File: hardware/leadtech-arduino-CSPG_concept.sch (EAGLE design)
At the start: 51 parts, among them IC1 CD4050B, IC2 LM358D, J1 CON_HEADER_1X08-PTH, J2 CON_HEADER_1X08-PTH, J3 CON_HEADER_1X08-PTH, J4 CON_HEADER_1X06-PTH, J5 CON_HEADER_1X05-PTH, J6 CON_HEADER_1X02-PTH, J7 CON_HEADER_1X05-PTH, J8 CON_HEADER_1X08-PTH, J9 CON_HEADER_1X02-PTH, P1 CON_HEADER_2X09, P2 CON_HEADER_2X09, Q1 16Mhz, SW1 SW_TACT_2P-3X6, U1 DS1302, U2 MFRC522, U3 PL2303HX

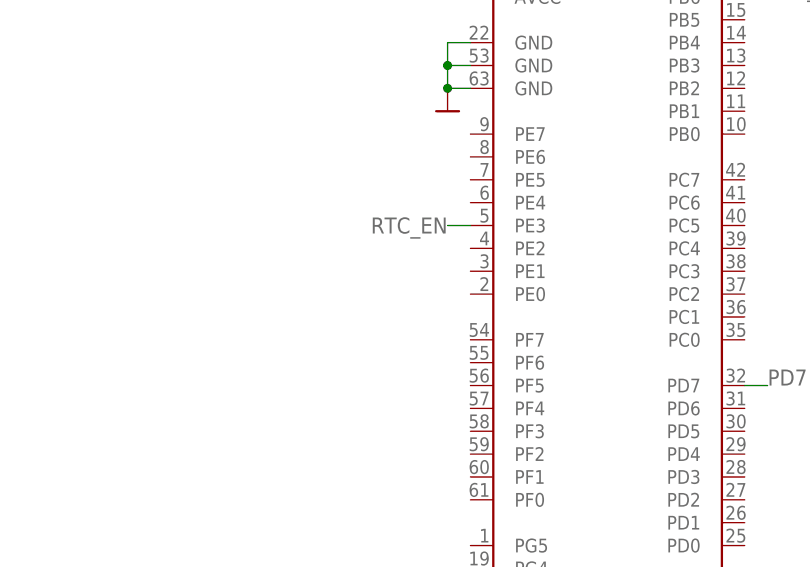
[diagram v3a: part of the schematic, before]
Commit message: continue wiring schematic
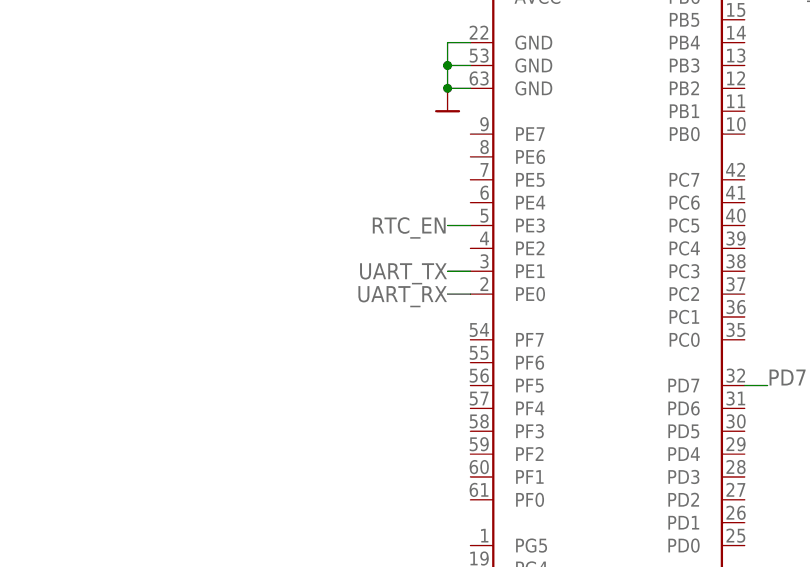
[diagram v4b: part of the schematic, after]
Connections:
- net UART_RX: now also U$1.PE0
- net UART_TX: now also U$1.PE1
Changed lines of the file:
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@@
 <label x="116.84" y="55.88" size="1.778" layer="95"/>
+</segment>
+<segment>
+<pinref part="U$1" gate="U" pin="PE0"/>
+<wire x1="383.54" y1="83.82" x2="381" y2="83.82" width="0.1524" layer="91"/>
+<label x="381" y="83.82" size="1.778" layer="95" align="center-right"/>
 </segment>
 </net>
@@
 <label x="116.84" y="48.26" size="1.778" layer="95"/>
 </segment>
+<segment>
+<pinref part="U$1" gate="U" pin="PE1"/>
+<wire x1="383.54" y1="86.36" x2="381" y2="86.36" width="0.1524" layer="91"/>
+<label x="381" y="86.36" size="1.778" layer="95" align="center-right"/>
+</segment>
 </net>

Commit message: add project schedule excel, add RFID module on schematic
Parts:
- removed U2: MFRC522, trosh_devices.eagle.v9:MFRC522
- added MOD1: RFIO-RC522, trosh_devices.eagle.v9:RFIO-RC522
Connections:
- net GND: now also MOD1.GND
- net N$1: now also MOD1.+3V3; no longer J8.8
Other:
- note added: "RFID MODULE"
- note added: "TO DO: wire RFID Module"
- note removed: "TO DO: connect RX and TX"
- moved on the sheet: C1, C10, G1, IC1P, R5, U1, XTAL1, ZD1

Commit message: continue wiring schematic, RFIF wiring done, level shifter done, add BOM with links on excel sheet
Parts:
- removed C1: 0.1uF, dp_devices.v6:CAPACITOR_NPOL-PTH_0.1"
- removed IC1: CD4050B, 40xx:4050N
- removed IC2: LM358D, linear:LM358D
- removed J7: CON_HEADER_1X05-PTH, dp_devices.v6:CON_HEADER_1X05-PTH
- removed J8: CON_HEADER_1X08-PTH, dp_devices.v6:CON_HEADER_1X08-PTH
- removed LED1: (no value), dp_devices.v6:LED-5MM
- removed R2: 4.7K, dp_devices.v6:RESISTOR-0603
- removed SW1: SW_TACT_2P-3X6, dp_devices.v6:SW_TACT_2P-3X6
- removed ZD1: 3.3V, dp_devices.v6:ZENERSOD-123
- added C14: 100uF, dp_devices.v6:CAPACITOR_POL-CASE_B
- added C15: 0.1uF, rcl:C-EUC0603
- added IC3: 4050D, 40xx:4050D
- added SG1: F/TMB, buzzer:F/TMB
- R1: value 330R -> 10K; device dp_devices.v6:RESISTOR-0603 -> rcl:R-EU_R0603
- R5: value 4.7K -> 10K; device dp_devices.v6:RESISTOR-0603 -> rcl:R-EU_R0603
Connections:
- removed net ARDUINO-10: IC1A.I, J1.3
- removed net ARDUINO-12: J1.5, J8.4
- removed net ARDUINO-2: J2.3, R2.2, SW1.1
- removed net ARDUINO-3: J2.4, R1.1
- removed net ARDUINO-5: J2.6, J7.5
- removed net ARDUINO-6: J2.7, J7.4
- removed net ARDUINO-7: J2.8, J7.3
- removed net ARDUINO-9: IC1D.I, J1.2
- removed net N$2: IC1A.O, J8.1
- removed net N$3: IC1B.I, J1.6
- removed net N$4: IC1B.O, J8.2
- removed net N$5: IC1C.I, J1.4
- removed net N$6: IC1C.O, J8.3
- removed net N$7: IC1D.O, J8.7
- removed net N$9: LED1.A, R1.2
- new net +3V3: C14.+, C15.2, IC3P.VDD, MOD1.+3V3
- new net OUT1: U$1.PE5
- new net PIEZO: R1.1, U$1.PG5
- new net RFID_CLOCK: IC3B.I, U$1.PB1
- new net RFID_CLOCK_3V: IC3B.O, MOD1.SCK
- new net RFID_DATA: IC3A.I, U$1.PB0
- new net RFID_DATA_3V: IC3A.O, MOD1.SDA
- new net RFID_MISO: MOD1.MISO, U$1.PB3
- new net RFID_MOSI: IC3C.I, U$1.PB2
- new net RFID_MOSI_3V: IC3C.O, MOD1.MOSI
- new net RFID_RESET: IC3D.I, U$1.PB5
- new net RFID_RESET_3V: IC3D.O, MOD1.RST
- new net SW1: R5.1, U$1.PE4
- net +5V: now also R5.2; no longer J7.1, LED2.A, R2.1, R5.1
- net GND: now also C14.-, C15.1, IC3P.VSS, SG1.-; no longer C1.2, IC1P.VSS, J7.2, J8.6, LED1.C, SW1.3, ZD1.A
- net N$1: now also R1.2, SG1.+; no longer C1.1, IC1P.VDD, MOD1.+3V3, R5.2, ZD1.C
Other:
- note added: "5V - 3.3V LEVEL SHIFTER"
- note added: "ARDUINO / ATMEGA1281"
- note added: "TO DO: change to HC-49S (PTH)"
- note added: "TO DO: place DC-DC power supply"
- note added: "TO DO: which USB connector?"
- note added: "VREGS"
- note removed: "3.3V"
- note removed: "CLK"
- note removed: "DAT"
- note removed: "IRQ"
- note removed: "MISO"
- note removed: "MOSI"
- note removed: "OUTPUT"
- note removed: "POWER SUPPLY"
- note removed: "RF-ID"
- note removed: "RST"
- note removed: "RTC"
- note removed: "SCK"
- note removed: "SDA"
- note removed: "SWITCH"
- note removed: "UC"
- moved on the sheet: C10, C8, C9, D1, G1, J9, LED2, MOD1, R9, U1, VREG1, XTAL1

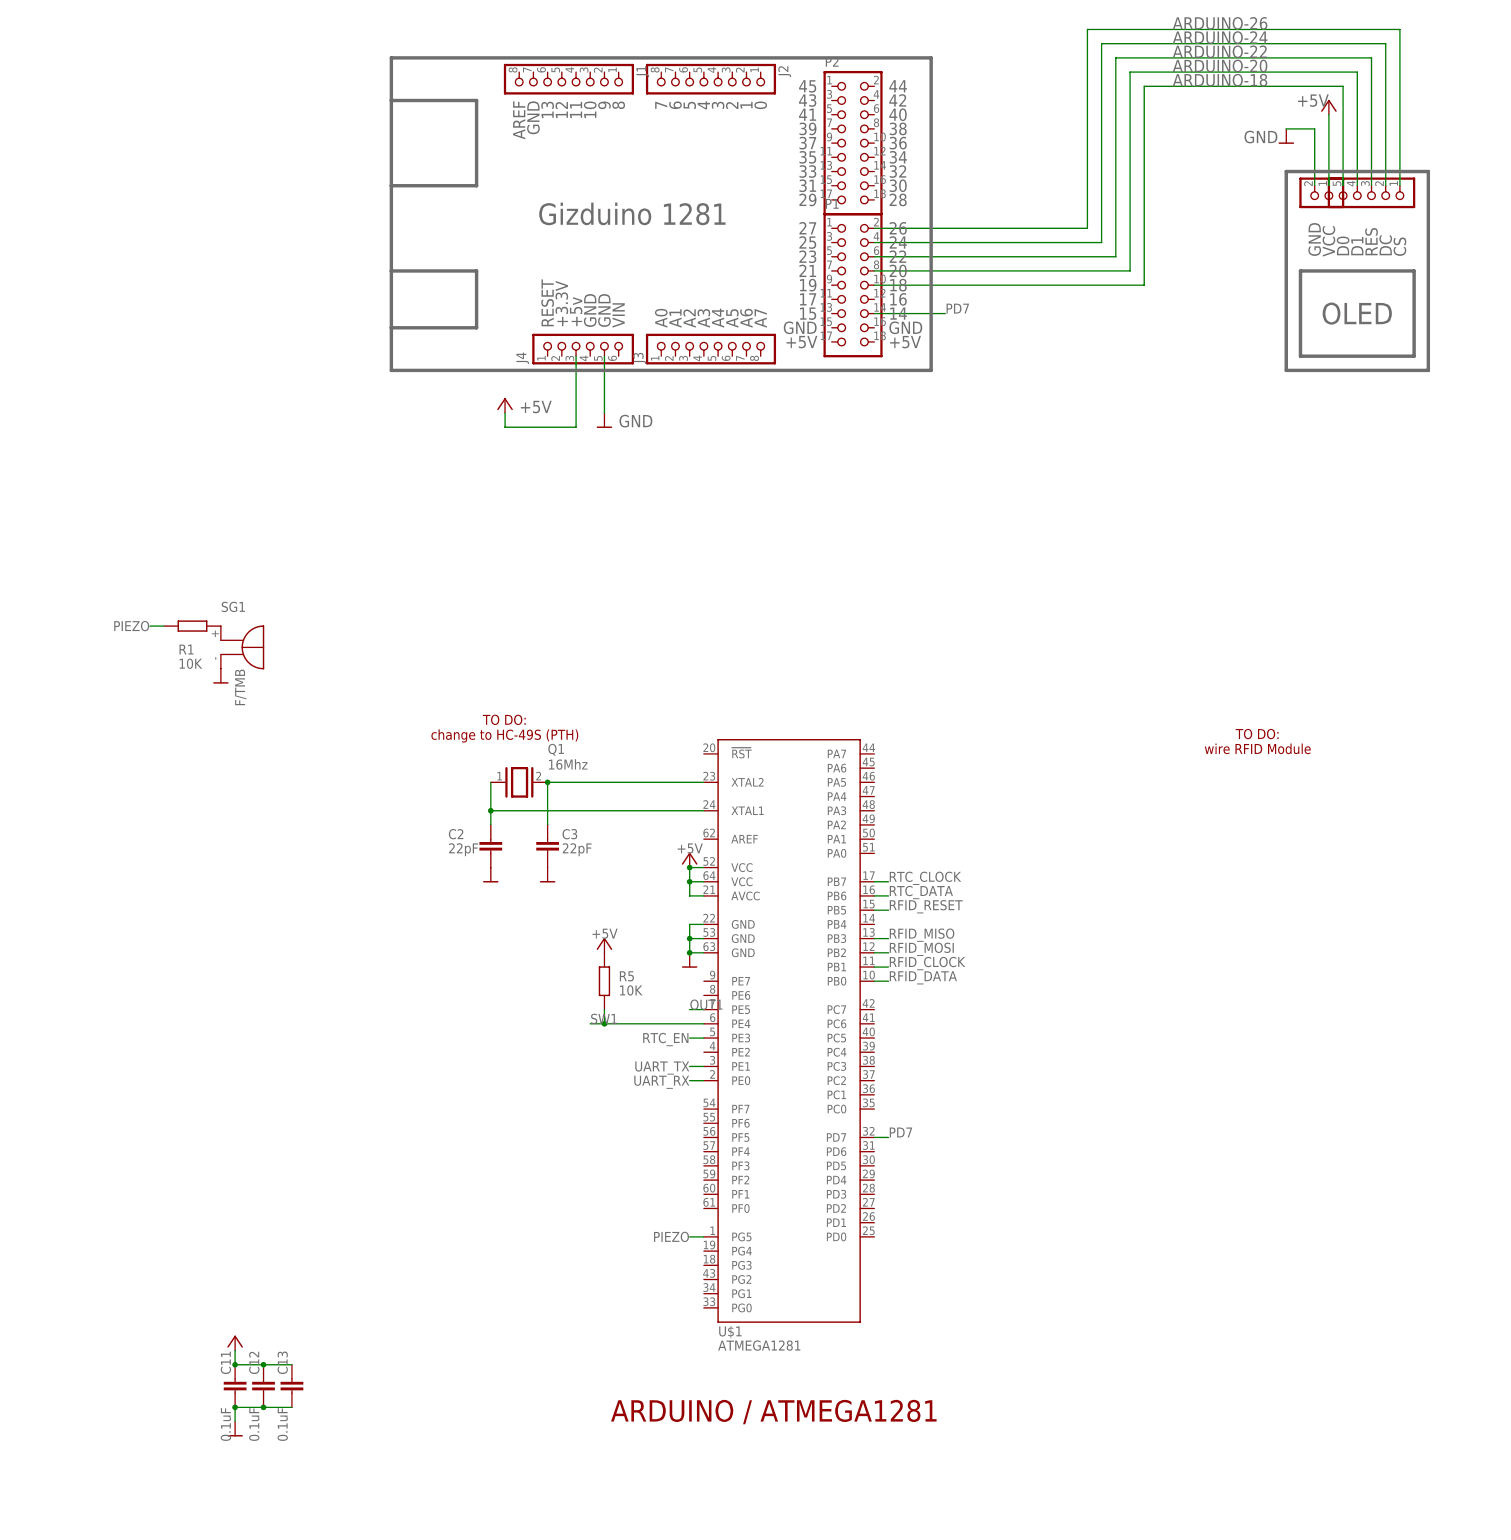
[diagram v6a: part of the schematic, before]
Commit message: continue on schematic work, add i2c OLED
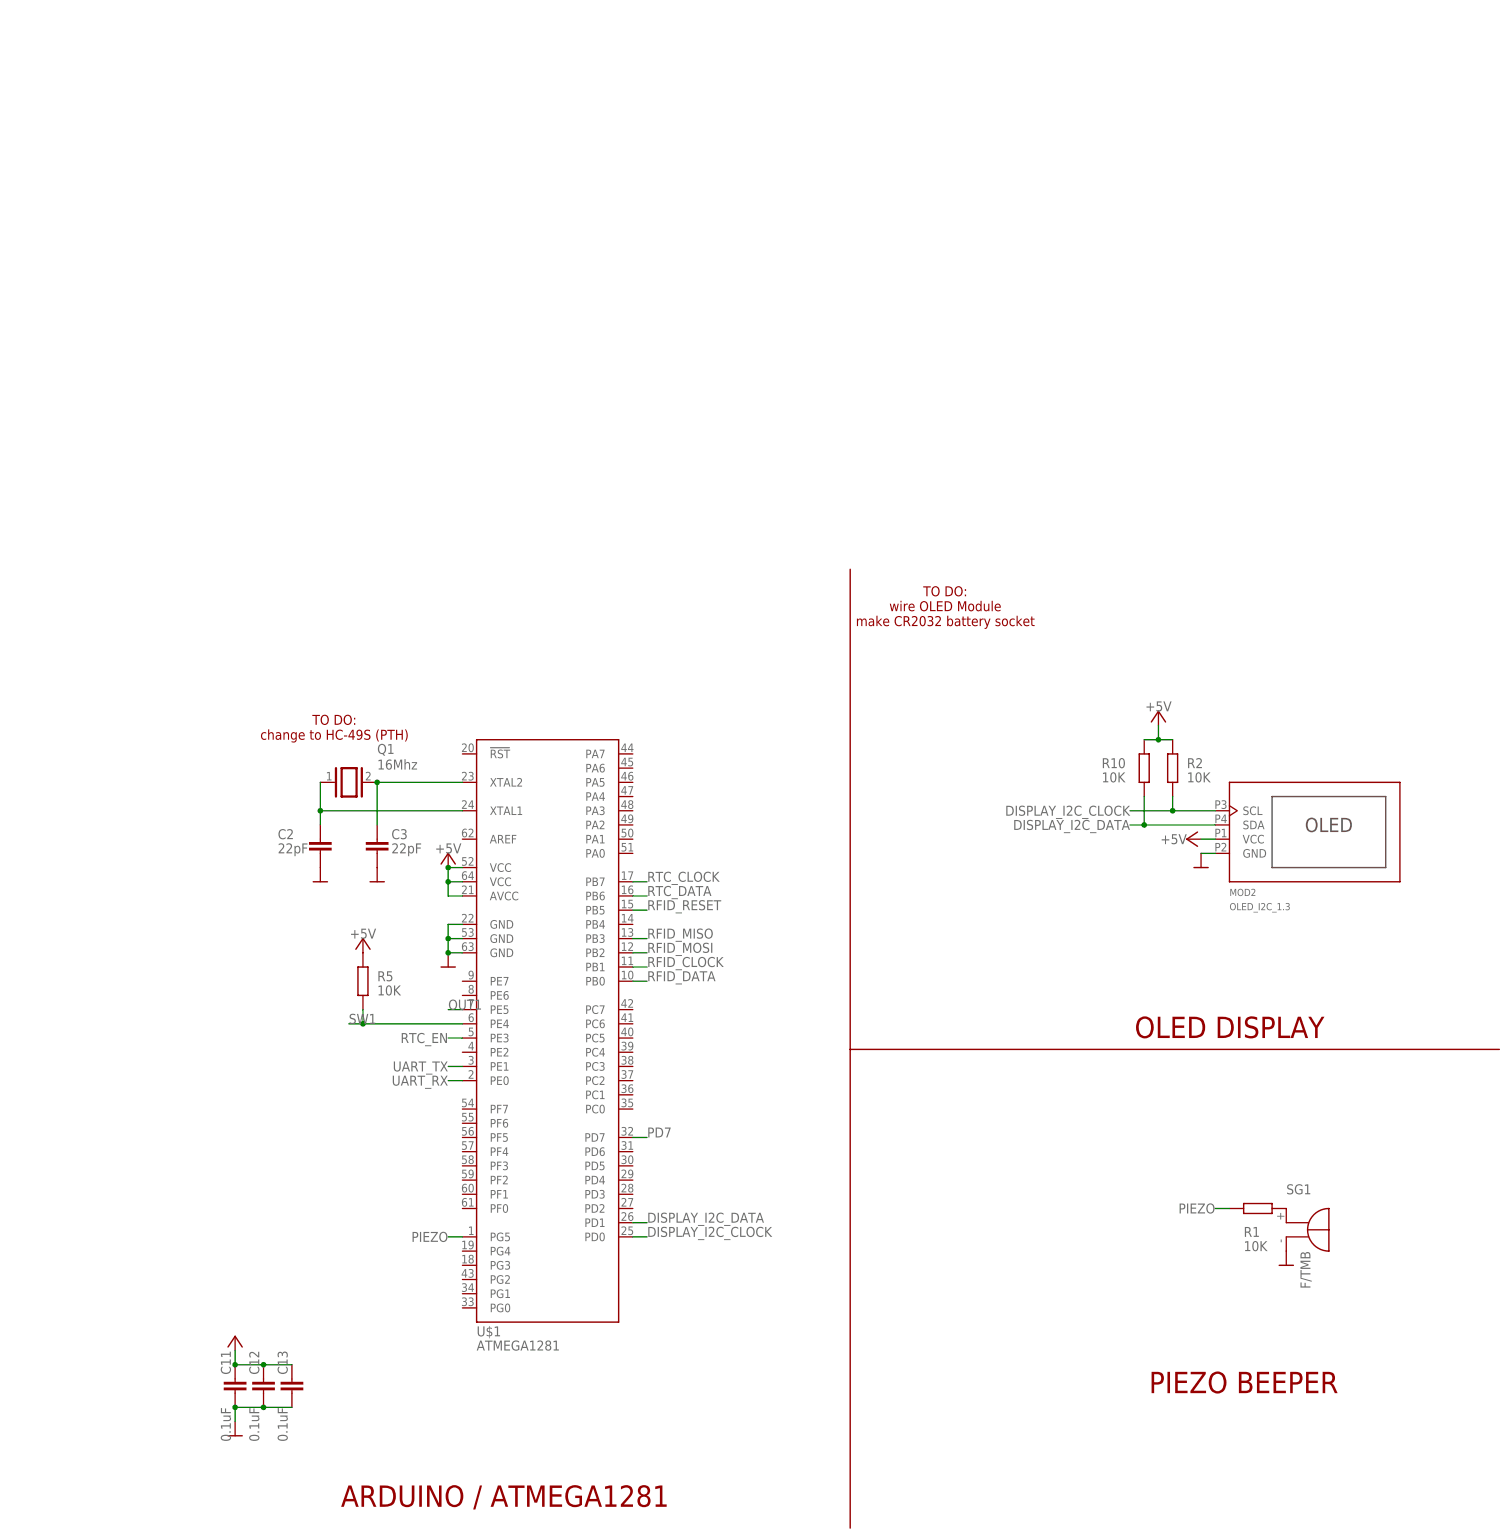
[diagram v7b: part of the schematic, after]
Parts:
- removed J1, J2, J3: CON_HEADER_1X08-PTH, dp_devices.v6:CON_HEADER_1X08-PTH
- removed J4: CON_HEADER_1X06-PTH, dp_devices.v6:CON_HEADER_1X06-PTH
- removed J5: CON_HEADER_1X05-PTH, dp_devices.v6:CON_HEADER_1X05-PTH
- removed J6: CON_HEADER_1X02-PTH, dp_devices.v6:CON_HEADER_1X02-PTH
- removed P1, P2: CON_HEADER_2X09, dp_devices.v6:CON_HEADER_2X09
- added MOD2: OLED_I2C_1.3, trosh_devices.eagle.v9:OLED_I2C_1.3
- added R10, R2: 10K, rcl:R-EU_R0603
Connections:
- removed net ARDUINO-18: J5.5, P1.10
- removed net ARDUINO-20: J5.4, P1.8
- removed net ARDUINO-22: J5.3, P1.6
- removed net ARDUINO-24: J5.2, P1.4
- removed net ARDUINO-26: J5.1, P1.2
- new net DISPLAY_I2C_CLOCK: MOD2.SCL, R2.1, U$1.PD0
- new net DISPLAY_I2C_DATA: MOD2.SDA, R10.1, U$1.PD1
- net +5V: now also MOD2.VCC, R10.2, R2.2; no longer J4.3, J6.1
- net GND: now also MOD2.GND; no longer J4.5, J6.2
- net PD7: no longer P1.14
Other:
- note added: "OLED DISPLAY"
- note added: "PIEZO BEEPER"
- note added: "TO DO: wire OLED Module make CR2032 battery socket"
- note removed: "+3.3V"
- note removed: "+5V"
- note removed: "+5v"
- note removed: "0"
- note removed: "1"
- note removed: "10"
- note removed: "11"
- note removed: "12"
- note removed: "13"
- note removed: "14"
- note removed: "15"
- note removed: "16"
- note removed: "17"
- note removed: "18"
- note removed: "19"
- note removed: "2"
- note removed: "20"
- note removed: "21"
- note removed: "22"
- note removed: "23"
- note removed: "24"
- note removed: "25"
- note removed: "26"
- note removed: "27"
- note removed: "28"
- note removed: "29"
- note removed: "3"
- note removed: "30"
- note removed: "31"
- note removed: "32"
- note removed: "33"
- note removed: "34"
- note removed: "35"
- note removed: "36"
- note removed: "37"
- note removed: "38"
- note removed: "39"
- note removed: "4"
- note removed: "40"
- note removed: "41"
- note removed: "42"
- note removed: "43"
- note removed: "44"
- note removed: "45"
- note removed: "5"
- note removed: "6"
- note removed: "7"
- note removed: "8"
- note removed: "9"
- note removed: "A0"
- note removed: "A1"
- note removed: "A2"
- note removed: "A3"
- note removed: "A4"
- note removed: "A5"
- note removed: "A6"
- note removed: "A7"
- note removed: "AREF"
- note removed: "CS"
- note removed: "D0"
- note removed: "D1"
- note removed: "DC"
- note removed: "GND"
- note removed: "Gizduino 1281"
- note removed: "OLED"
- note removed: "RES"
- note removed: "RESET"
- note removed: "TO DO: wire RFID Module"
- note removed: "VCC"
- note removed: "VIN"
- moved on the sheet: C2, C3, Q1, R1, R5, SG1, U$1

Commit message: edited box plate drawing, added chip docs
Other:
- note added: "TO DO: make CR2032 battery socket make circuit for the control relay build DC-DC for power supply"
- note removed: "TO DO: wire OLED Module make CR2032 battery socket"
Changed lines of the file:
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@@
 <wire x1="130.302" y1="99.568" x2="3.81" y2="99.568" width="0.254" layer="94"/>
 <text x="347.98" y="7.62" size="3.81" layer="94" ratio="12" align="bottom-center">ARDUINO / ATMEGA1281</text>
-<text x="426.72" y="165.1" size="1.778" layer="94" ratio="12" align="bottom-center">TO DO:
-wire OLED Module
-make CR2032 battery socket</text>
+<text x="426.72" y="165.1" size="1.778" layer="94" ratio="12" align="top-left">TO DO:
+make CR2032 battery socket
+make circuit for the control relay
+build DC-DC for power supply</text>
 <text x="231.14" y="104.14" size="3.81" layer="94" ratio="12" align="bottom-center">RFID MODULE</text>
 <wire x1="256.54" y1="99.568" x2="203.962" y2="99.568" width="0.254" layer="94"/>
